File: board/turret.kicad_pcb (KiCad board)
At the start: 2 copper layers, 56 x 32 mm, 51 parts, among them M1 SRV_LAS, M2 SRV_SEN, Q1 BC848, SW1 SW_Push, U1 STM32F103CBTx, U2 W25Q16JLSSIG, U3 TPA2005D1DGN, U4 TPS61322xADBV, U5 TLV70028_SOT23-5

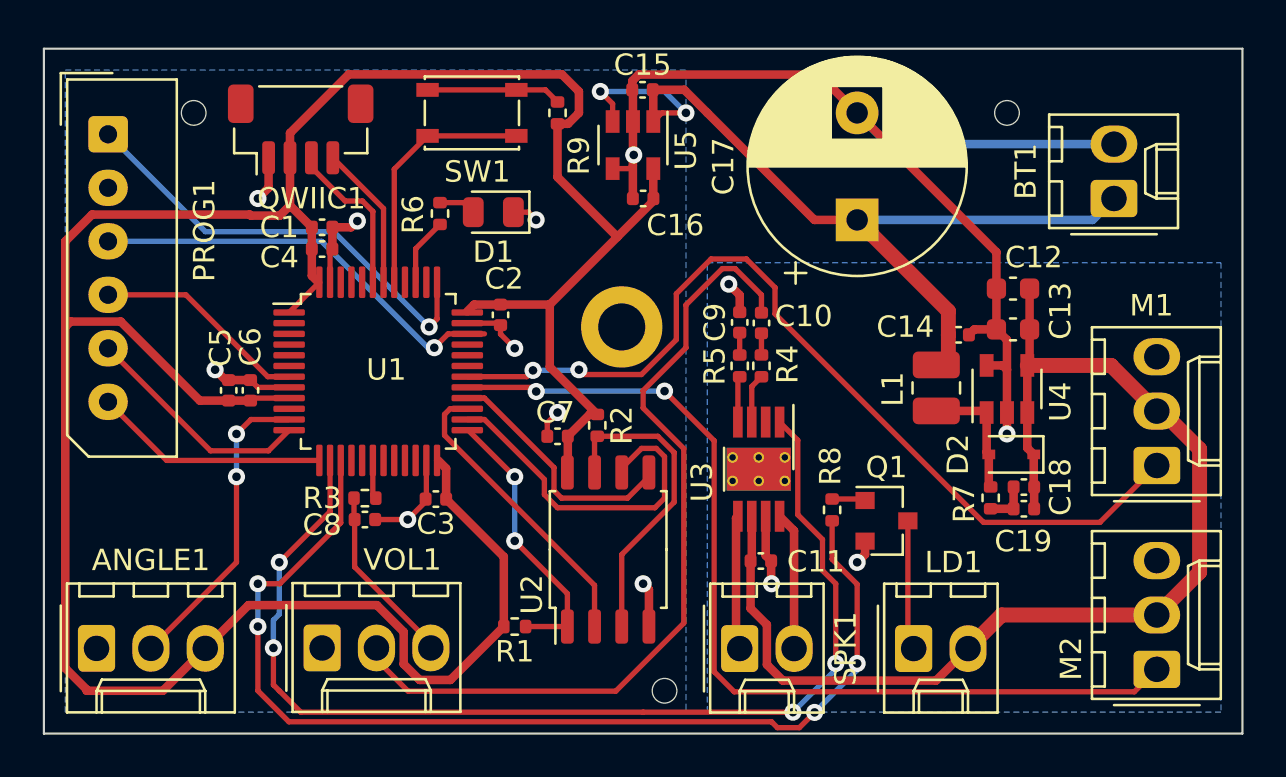
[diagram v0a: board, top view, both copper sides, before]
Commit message: Adjust component clearances for assembly
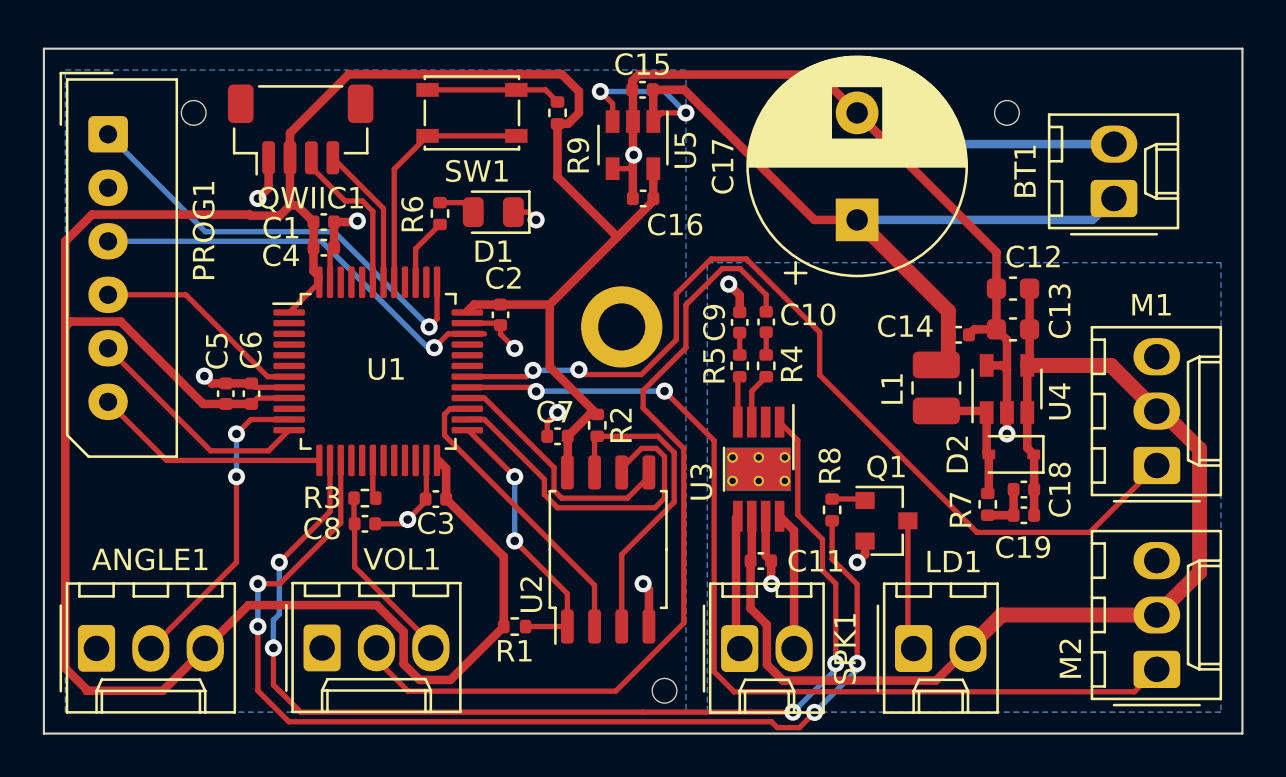
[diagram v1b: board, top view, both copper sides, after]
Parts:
- moved R7 0.33 mm to (171.1, 98.3)
- moved C19 0.30 mm to (172.8, 98.8)
- moved C1 0.26 mm to (140.1, 85.1)
- moved C10 0.23 mm to (160.8, 89.8)
- moved R4 0.22 mm to (160.8, 91.8)
- moved C5 0.21 mm to (135.5, 93.1)
- moved C8 0.20 mm to (142.0, 99.2)
- moved C6 0.16 mm to (136.7, 93.1)
- moved C18 0.12 mm to (172.8, 97.6)
- moved C4 0.10 mm to (140.1, 86.3)
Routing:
- net /SRV_LAS: track 42.9 -> 43.7 mm
- net GNDA: track 78.8 -> 79.3 mm
